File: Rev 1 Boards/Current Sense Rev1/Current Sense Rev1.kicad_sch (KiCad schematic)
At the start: 0 parts

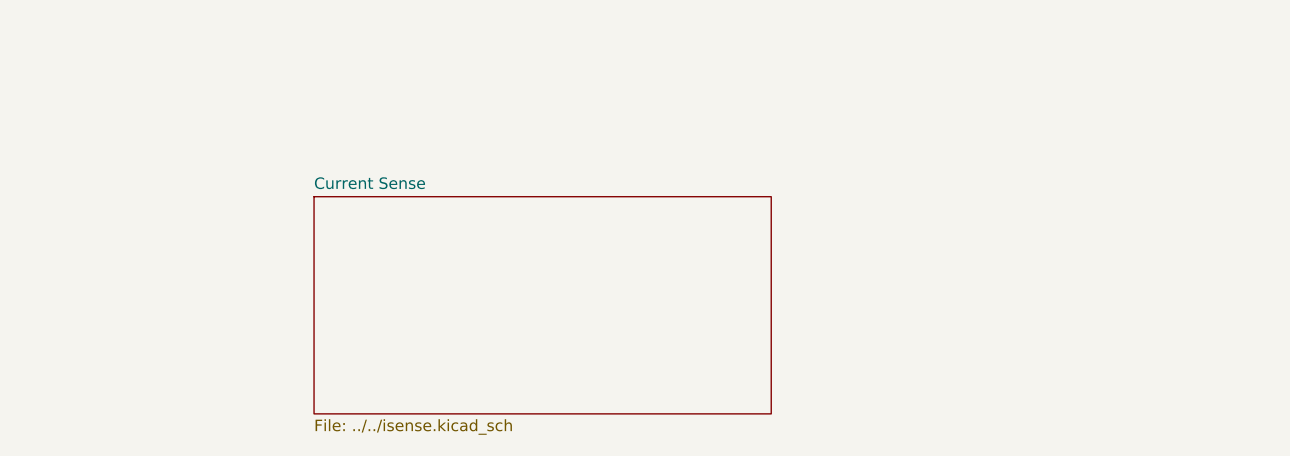
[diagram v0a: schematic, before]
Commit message: current sense PCB layout
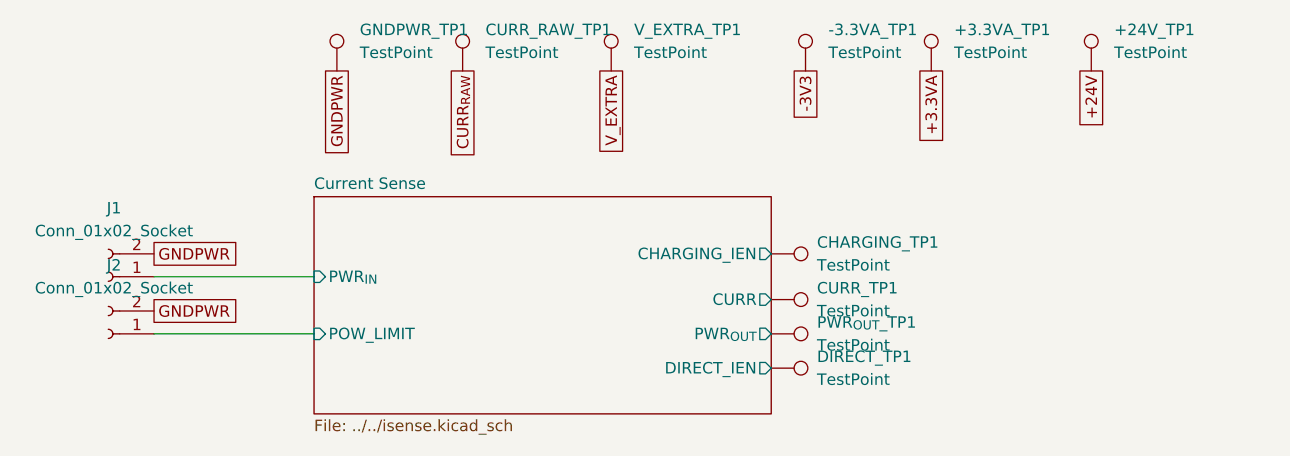
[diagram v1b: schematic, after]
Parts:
- added +24V_TP1, +3.3VA_TP1, -3.3VA_TP1, CHARGING_TP1, CURR_RAW_TP1, CURR_TP1, DIRECT_TP1, GNDPWR_TP1, PWR_{OUT}_TP1, V_EXTRA_TP1: TestPoint, TestPoint:TestPoint_Keystone_5010-5014_Multipurpose, symbol Connector:TestPoint
- added J1, J2: Conn_01x02_Socket, Connector:Banana_Jack_2Pin, symbol Connector:Conn_01x02_Socket
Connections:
- new net +24V: +24V_TP1.1
- new net +3.3VA: +3.3VA_TP1.1
- new net -3V3: -3.3VA_TP1.1
- new net CURR_{RAW}: CURR_RAW_TP1.1
- new net Current Sense/CHARGING_IEN: CHARGING_TP1.1
- new net Current Sense/CURR: CURR_TP1.1
- new net Current Sense/DIRECT_IEN: DIRECT_TP1.1
- new net Current Sense/POW_LIMIT: J2.1 (Pin_1)
- new net Current Sense/PWR_{IN}: J1.1 (Pin_1)
- new net Current Sense/PWR_{OUT}: PWR_{OUT}_TP1.1
- new net GNDPWR: GNDPWR_TP1.1, J1.2 (Pin_2), J2.2 (Pin_2)
- new net V_EXTRA: V_EXTRA_TP1.1
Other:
- sheet Current Sense ports: added CHARGING_IEN, CURR, DIRECT_IEN, POW_LIMIT, PWR_{IN}, PWR_{OUT}; removed none

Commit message: modified tracks
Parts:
- removed PWR_{OUT}_TP1: TestPoint, TestPoint:TestPoint_Keystone_5010-5014_Multipurpose, symbol Connector:TestPoint
- added J3: Conn_01x02_Socket, Connector:Banana_Jack_2Pin, symbol Connector:Conn_01x02_Socket
- renumbered CURR_TP1 to ADC_CURR1, CHARGING_TP1 to CHARGING_OUT1, CURR_RAW_TP1 to CURR_RAW1, DIRECT_TP1 to DIRECT_OUT1, GNDPWR_TP1 to GNDPWR1, V_EXTRA_TP1 to SCHMITT_V_IN1
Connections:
- net Current Sense/PWR_{OUT}: now also J3.1 (Pin_1)
- net GNDPWR: now also J3.2 (Pin_2)
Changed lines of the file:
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@@
+		)
+	)
+	(wire
+		(pts
+			(xy 121.92 97.79) (xy 149.86 97.79)
+		)
+		(stroke
+			(width 0)
+			(type default)
 		)
 	)
@@
 		)
 	)
+	(global_label "GNDPWR"
+		(shape passive)
+		(at 149.86 100.33 180)
+		(fields_autoplaced yes)
+		(effects
+			(font
+				(size 1.27 1.27)
+			)
+			(justify right)
+		)
+		(property "Intersheetrefs" "${INTERSHEET_REFS}"
+			(at 140.1242 100.33 0)
+			(effects
+				(font
+					(size 1.27 1.27)
+				)
+				(justify right)
+				(hide yes)
+			)
+		)
+	)
 	(symbol
 		(lib_id "Connector:TestPoint")
@@
 		(dnp no)
 		(fields_autoplaced yes)
-		(property "Reference" "V_EXTRA_TP1"
+		(property "Reference" "SCHMITT_V_IN1"
 			(at 106.68 64.0079 0)
 			(effects
@@
 			(project "Current Sense Rev1"
 				(path "/d149d1fa-5de7-4dc0-b1ef-e9c4223d2865"
-					(reference "V_EXTRA_TP1")
+					(reference "SCHMITT_V_IN1")
 					(unit 1)
 				)
@@
 		(dnp no)
 		(fields_autoplaced yes)
-		(property "Reference" "CURR_TP1"
+		(property "Reference" "ADC_CURR1"
 			(at 127 92.7099 90)
 			(effects
@@
 			(project "Current Sense Rev1"
 				(path "/d149d1fa-5de7-4dc0-b1ef-e9c4223d2865"
-					(reference "CURR_TP1")
+					(reference "ADC_CURR1")
 					(unit 1)
 				)
@@
 		(dnp no)
 		(fields_autoplaced yes)
-		(property "Reference" "CHARGING_TP1"
+		(property "Reference" "CHARGING_OUT1"
 			(at 127 87.6299 90)
 			(effects
@@
 			(project "Current Sense Rev1"
 				(path "/d149d1fa-5de7-4dc0-b1ef-e9c4223d2865"
-					(reference "CHARGING_TP1")
+					(reference "CHARGING_OUT1")
+					(unit 1)
+				)
+			)
+		)
+	)
+	(symbol
+		(lib_id "Connector:Conn_01x02_Socket")
+		(at 154.94 97.79 0)
+		(unit 1)
+		(exclude_from_sim no)
+		(in_bom yes)
+		(on_board yes)
+		(dnp no)
+		(fields_autoplaced yes)
+		(property "Reference" "J3"
+			(at 156.21 97.7899 0)
+			(effects
+				(font
+					(size 1.27 1.27)
+				)
+				(justify left)
+			)
+		)
+		(property "Value" "Conn_01x02_Socket"
+			(at 156.21 100.3299 0)
+			(effects
+				(font
+					(size 1.27 1.27)
+				)
+				(justify left)
+			)
+		)
+		(property "Footprint" "Connector:Banana_Jack_2Pin"
+			(at 154.94 97.79 0)
+			(effects
+				(font
+					(size 1.27 1.27)
+				)
+				(hide yes)
+			)
+		)
+		(property "Datasheet" "~"
+			(at 154.94 97.79 0)
+			(effects
+				(font
+					(size 1.27 1.27)
+				)
+				(hide yes)
+			)
+		)
+		(property "Description" "Generic connector, single row, 01x02, script generated"
+			(at 154.94 97.79 0)
+			(effects
+				(font
+					(size 1.27 1.27)
+				)
+				(hide yes)
+			)
+		)
+		(pin "2"
+		)
+		(pin "1"
+		)
+		(instances
+			(project "Current Sense Rev1"
+				(path "/d149d1fa-5de7-4dc0-b1ef-e9c4223d2865"
+					(reference "J3")
 					(unit 1)
 				)
@@
 		(dnp no)
 		(fields_autoplaced yes)
-		(property "Reference" "CURR_RAW_TP1"
+		(property "Reference" "CURR_RAW1"
 			(at 90.17 64.0079 0)
 			(effects
@@
 			(project "Current Sense Rev1"
 				(path "/d149d1fa-5de7-4dc0-b1ef-e9c4223d2865"
-					(reference "CURR_RAW_TP1")
+					(reference "CURR_RAW1")
 					(unit 1)
 				)
@@
 		(dnp no)
 		(fields_autoplaced yes)
-		(property "Reference" "DIRECT_TP1"
+		(property "Reference" "DIRECT_OUT1"
 			(at 127 100.3299 90)
 			(effects
@@
 			(project "Current Sense Rev1"
 				(path "/d149d1fa-5de7-4dc0-b1ef-e9c4223d2865"
-					(reference "DIRECT_TP1")
+					(reference "DIRECT_OUT1")
 					(unit 1)
 				)
@@
 		(dnp no)
 		(fields_autoplaced yes)
-		(property "Reference" "GNDPWR_TP1"
+		(property "Reference" "GNDPWR1"
 			(at 76.2 64.0079 0)
 			(effects
@@
 			(project "Current Sense Rev1"
 				(path "/d149d1fa-5de7-4dc0-b1ef-e9c4223d2865"
-					(reference "GNDPWR_TP1")
-					(unit 1)
-				)
-			)
-		)
-	)
-	(symbol
-		(lib_id "Connector:TestPoint")
-		(at 121.92 97.79 270)
-		(unit 1)
-		(exclude_from_sim no)
-		(in_bom yes)
-		(on_board yes)
-		(dnp no)
-		(fields_autoplaced yes)
-		(property "Reference" "PWR_{OUT}_TP1"
-			(at 127 96.5199 90)
-			(effects
-				(font
-					(size 1.27 1.27)
-				)
-				(justify left)
-			)
-		)
-		(property "Value" "TestPoint"
-			(at 127 99.0599 90)
-			(effects
-				(font
-					(size 1.27 1.27)
-				)
-				(justify left)
-			)
-		)
-		(property "Footprint" "TestPoint:TestPoint_Keystone_5010-5014_Multipurpose"
-			(at 121.92 102.87 0)
-			(effects
-				(font
-					(size 1.27 1.27)
-				)
-				(hide yes)
-			)
-		)
-		(property "Datasheet" "~"
-			(at 121.92 102.87 0)
-			(effects
-				(font
-					(size 1.27 1.27)
-				)
-				(hide yes)
-			)
-		)
-		(property "Description" "test point"
-			(at 121.92 97.79 0)
-			(effects
-				(font
-					(size 1.27 1.27)
-				)
-				(hide yes)
-			)
-		)
-		(pin "1"
-		)
-		(instances
-			(project "Current Sense Rev1"
-				(path "/d149d1fa-5de7-4dc0-b1ef-e9c4223d2865"
-					(reference "PWR_{OUT}_TP1")
-					(unit 1)
-				)
+					(reference "GNDPWR1")
+					(unit 1)
+				)
